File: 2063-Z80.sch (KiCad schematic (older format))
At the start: 94 parts, among them J1 Conn_01x05, J10 Conn_01x07, J11 Conn_02x03, J12 Conn_01x02, J13 Conn_01x06, J14 Conn_01x02, J2 DM3D-SF(41), J3 Conn_02x20, J4 Conn_02x05, J5 Conn_02x05, J6 0548190519, J7 Conn_02x13, J8 Conn_01x05, J9 Conn_01x02, Q1 PN2222, U1 Z80-CPU, U10 74HC32, U11 74HCT132, U12 ICL3232CPZ, U13 74HC32, U2 AS6C4008-55PCN, U20 LM1117-3.3, U3 SST39SF010, U4 Z80-CTC, U5 Z80-SIO-0, U6 74HC374, U7 74HC374, U8 74LS244, U9 74HC138, X1 ACH-10.000MHZ-EK, X2 ECS-2100A-018

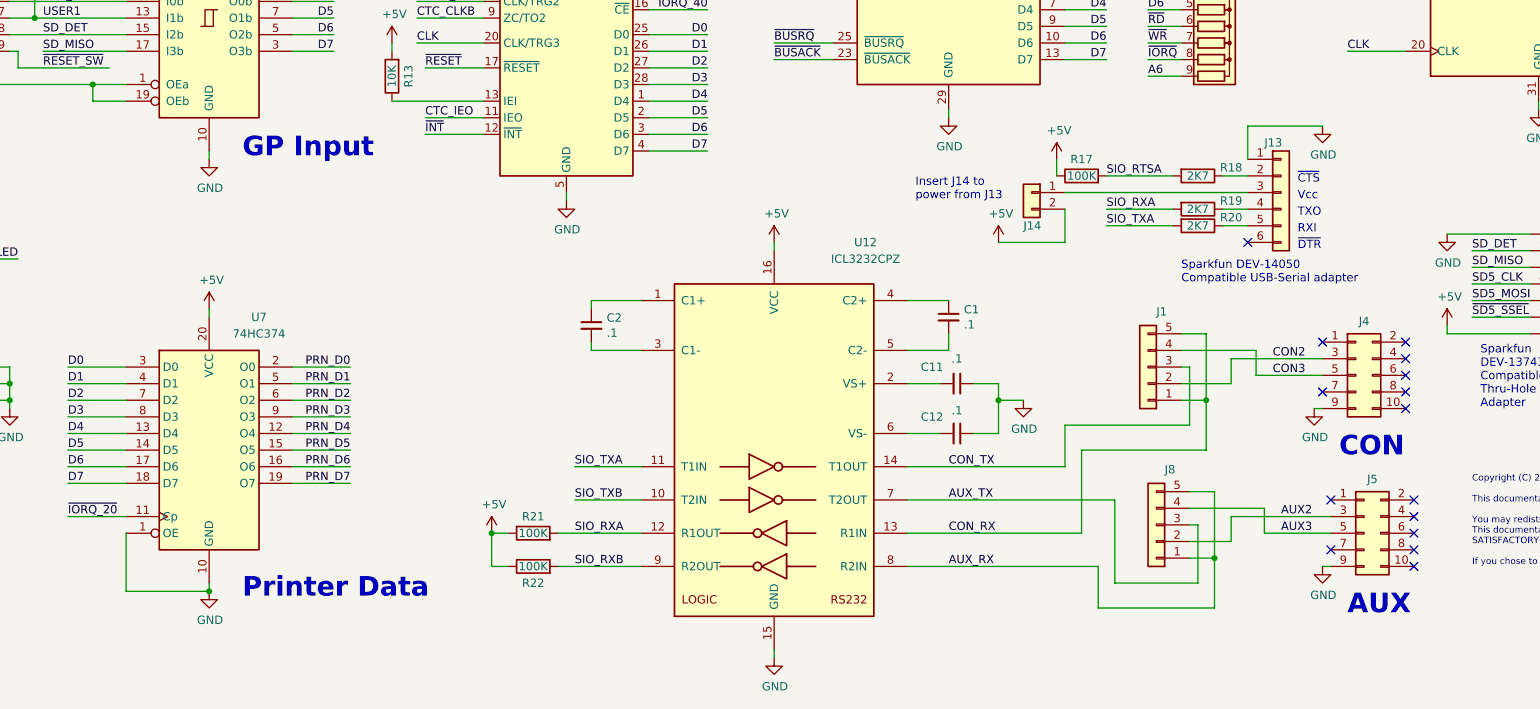
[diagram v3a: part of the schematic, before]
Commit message: Mark optional USB bits
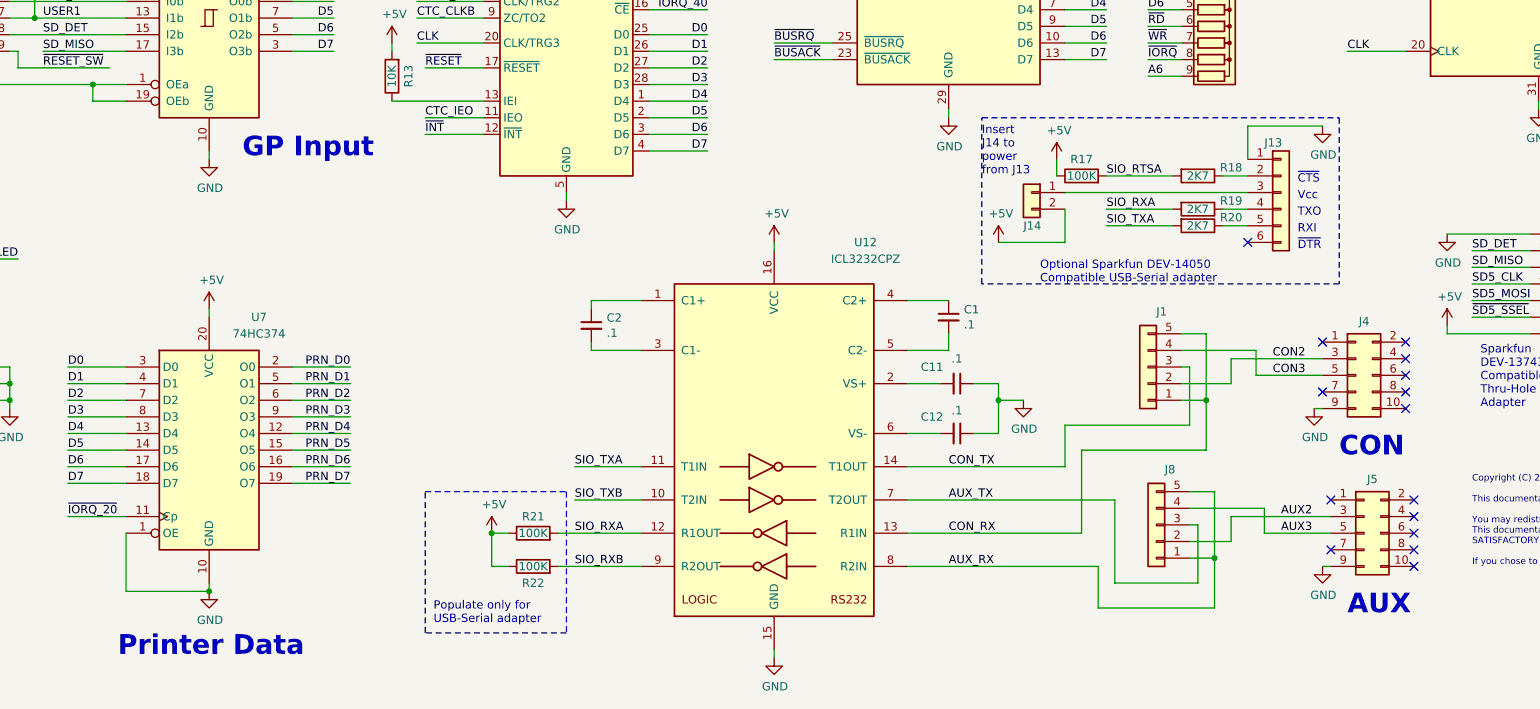
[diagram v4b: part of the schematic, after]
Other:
- note added: "Insert\nJ14 to\npower\nfrom J13"
- note added: "Optional Sparkfun DEV-14050\nCompatible USB-Serial adapter"
- note added: "Populate only for \nUSB-Serial adapter"
- note removed: "Insert J14 to\npower from J13\n"
- note removed: "Sparkfun DEV-14050\nCompatible USB-Serial adapter"
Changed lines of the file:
@@
 Text Notes 1500 10050 0    118  ~ 24
 GP Output
-Text Notes 4900 10050 0    118  ~ 24
+Text Notes 4150 10400 0    118  ~ 24
 Printer Data
 Text Notes 14400 4550 0    118  ~ 24
@@
 	1    0    0    -1
 $EndComp
-Text Notes 10550 8150 0    50   ~ 0
-Sparkfun DEV-14050\nCompatible USB-Serial adapter
+Text Notes 9700 8150 0    50   ~ 0
+Optional Sparkfun DEV-14050\nCompatible USB-Serial adapter
 $Comp
 L Connector_Generic:Conn_01x06 J13
@@
 	1    0    0    -1
 $EndComp
-Text Notes 8950 7650 0    50   ~ 0
-Insert J14 to\npower from J13\n
+Text Notes 9350 7500 0    50   ~ 0
+Insert\nJ14 to\npower\nfrom J13
 Text Notes 11250 7850 0    50   ~ 0
 RXI
@@
 	1    0    0    -1
 $EndComp
+Wire Notes Line
+	11500 7150 11500 8150
+Wire Notes Line
+	11500 8150 9350 8150
+Wire Notes Line
+	9350 8150 9350 7150
+Wire Notes Line
+	9350 7150 11500 7150
+Wire Notes Line
+	6000 9400 6850 9400
+Wire Notes Line
+	6850 9400 6850 10250
+Wire Notes Line
+	6850 10250 6000 10250
+Wire Notes Line
+	6000 10250 6000 9400
+Text Notes 6050 10200 0    50   ~ 0
+Populate only for \nUSB-Serial adapter
 $EndSCHEMATC

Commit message: Merge version 4.3 into main
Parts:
- removed J13: Conn_01x06, Connector_PinHeader_2.54mm:PinHeader_1x06_P2.54mm_Horizontal, symbol Connector_Generic:Conn_01x06
- removed J14: Conn_01x02, Connector_PinHeader_2.54mm:PinHeader_1x02_P2.54mm_Horizontal, symbol Connector_Generic:Conn_01x02
- removed R17, R21, R22: 100K, Resistor_THT:R_Axial_DIN0204_L3.6mm_D1.6mm_P5.08mm_Horizontal, symbol Device:R
- removed R18, R19, R20: 2K7, Resistor_THT:R_Axial_DIN0204_L3.6mm_D1.6mm_P5.08mm_Horizontal, symbol Device:R
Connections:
- net SIO_RTSA: no longer names the net of U5.17 (~RTSA)
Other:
- note removed: "Insert\nJ14 to\npower\nfrom J13"
- note removed: "Optional Sparkfun DEV-14050\nCompatible USB-Serial adapter"
- note removed: "Populate only for \nUSB-Serial adapter"
- note removed: "RXI"
- note removed: "TXO"
- note removed: "Vcc"
- note removed: "~CTS"
- note removed: "~DTR"
- moved on the sheet: J1, J4, RN2, RN4, RN5

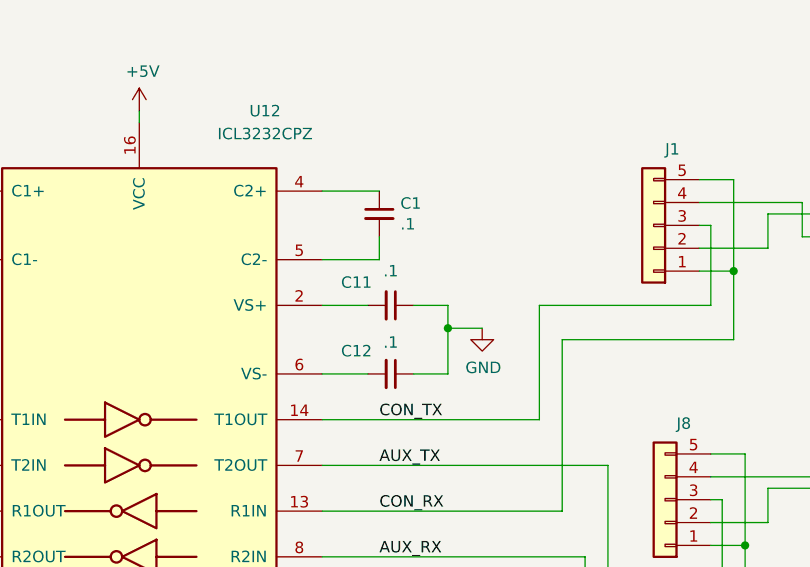
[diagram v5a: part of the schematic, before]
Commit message: Change C1, 11 and 12 to .47uF
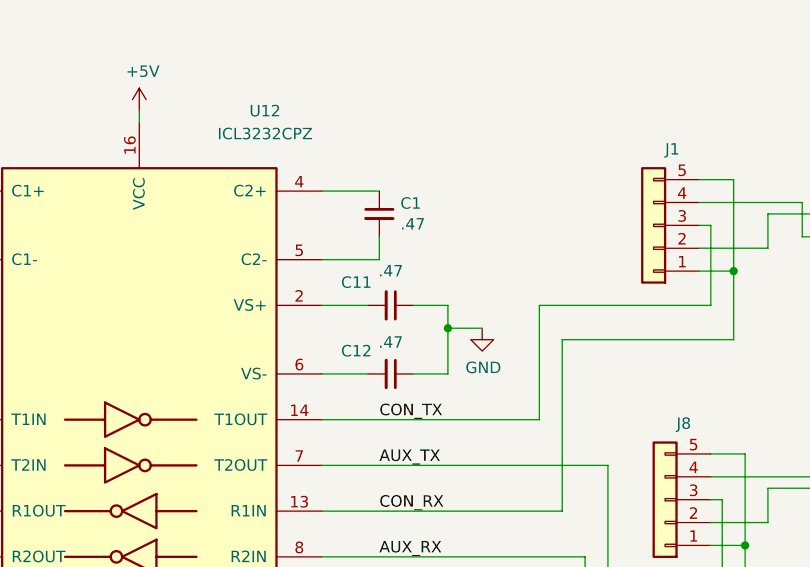
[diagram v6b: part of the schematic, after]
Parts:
- C1, C11, C12: value .1 -> .47; Description CAP CER 0.1UF 50V Z5U RADIAL -> CAP CER 0.47UF 50V X7R RADIAL; Digi-Key_PN 399-9859-1-ND -> 399-14039-1-ND; MPN ‎C315C104M5U5TA7303‎ -> C315C474K5R5TA7303
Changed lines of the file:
@@
 P 9150 8350
 F 0 "C1" H 9242 8396 50  0000 L CNN
-F 1 ".1" H 9242 8305 50  0000 L CNN
+F 1 ".47" H 9242 8305 50  0000 L CNN
 F 2 "Capacitor_THT:C_Disc_D3.0mm_W2.0mm_P2.50mm" H 9150 8350 50  0001 C CNN
-F 3 "https://api.kemet.com/component-edge/download/specsheet/C315C104M5U5TA7303.pdf" H 9150 8350 50  0001 C CNN
-F 4 "399-9859-1-ND" H 9150 8350 50  0001 C CNN "Digi-Key_PN"
-F 5 "‎C315C104M5U5TA7303‎" H 9150 8350 50  0001 C CNN "MPN"
-F 6 "CAP CER 0.1UF 50V Z5U RADIAL" H 9150 8350 50  0001 C CNN "Description"
+F 3 "https://api.kemet.com/component-edge/download/datasheet/C315C474K5R5TA7303.pdf" H 9150 8350 50  0001 C CNN
+F 4 "399-14039-1-ND" H 9150 8350 50  0001 C CNN "Digi-Key_PN"
+F 5 "C315C474K5R5TA7303" H 9150 8350 50  0001 C CNN "MPN"
+F 6 "CAP CER 0.47UF 50V X7R RADIAL" H 9150 8350 50  0001 C CNN "Description"
 F 7 "KEMET" H 9150 8350 50  0001 C CNN "Manufacturer"
 	1    9150 8350
@@
 P 9200 8750
 F 0 "C11" V 9100 8600 50  0000 C CNN
-F 1 ".1" V 9050 8750 50  0000 C CNN
+F 1 ".47" V 9050 8750 50  0000 C CNN
 F 2 "Capacitor_THT:C_Disc_D3.0mm_W2.0mm_P2.50mm" H 9200 8750 50  0001 C CNN
-F 3 "https://api.kemet.com/component-edge/download/specsheet/C315C104M5U5TA7303.pdf" H 9200 8750 50  0001 C CNN
-F 4 "399-9859-1-ND" H 9200 8750 50  0001 C CNN "Digi-Key_PN"
-F 5 "‎C315C104M5U5TA7303‎" H 9200 8750 50  0001 C CNN "MPN"
-F 6 "CAP CER 0.1UF 50V Z5U RADIAL" H 9200 8750 50  0001 C CNN "Description"
+F 3 "https://api.kemet.com/component-edge/download/datasheet/C315C474K5R5TA7303.pdf" H 9200 8750 50  0001 C CNN
+F 4 "399-14039-1-ND" H 9200 8750 50  0001 C CNN "Digi-Key_PN"
+F 5 "C315C474K5R5TA7303" H 9200 8750 50  0001 C CNN "MPN"
+F 6 "CAP CER 0.47UF 50V X7R RADIAL" H 9200 8750 50  0001 C CNN "Description"
 F 7 "KEMET" H 9200 8750 50  0001 C CNN "Manufacturer"
 	1    9200 8750
@@
 P 9200 9050
 F 0 "C12" V 9100 8900 50  0000 C CNN
-F 1 ".1" V 9062 9050 50  0000 C CNN
+F 1 ".47" V 9062 9050 50  0000 C CNN
 F 2 "Capacitor_THT:C_Disc_D3.0mm_W2.0mm_P2.50mm" H 9200 9050 50  0001 C CNN
-F 3 "https://api.kemet.com/component-edge/download/specsheet/C315C104M5U5TA7303.pdf" H 9200 9050 50  0001 C CNN
-F 4 "399-9859-1-ND" H 9200 9050 50  0001 C CNN "Digi-Key_PN"
-F 5 "‎C315C104M5U5TA7303‎" H 9200 9050 50  0001 C CNN "MPN"
-F 6 "CAP CER 0.1UF 50V Z5U RADIAL" H 9200 9050 50  0001 C CNN "Description"
+F 3 "https://api.kemet.com/component-edge/download/datasheet/C315C474K5R5TA7303.pdf" H 9200 9050 50  0001 C CNN
+F 4 "399-14039-1-ND" H 9200 9050 50  0001 C CNN "Digi-Key_PN"
+F 5 "C315C474K5R5TA7303" H 9200 9050 50  0001 C CNN "MPN"
+F 6 "CAP CER 0.47UF 50V X7R RADIAL" H 9200 9050 50  0001 C CNN "Description"
 F 7 "KEMET" H 9200 9050 50  0001 C CNN "Manufacturer"
 	1    9200 9050
